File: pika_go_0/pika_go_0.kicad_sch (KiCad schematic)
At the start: 0 parts

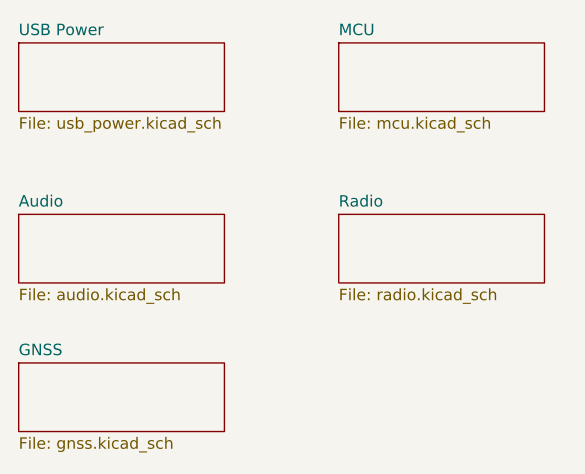
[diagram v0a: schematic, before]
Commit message: Libraries cleanup, schematics finished, copper tracing finished, still need some PCB cleanup
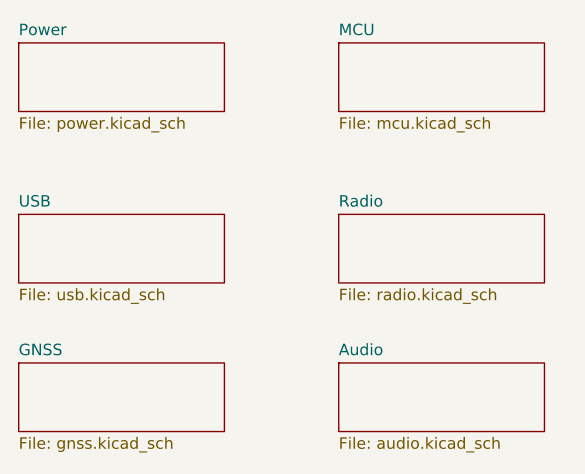
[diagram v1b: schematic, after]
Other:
- sheet USB Power renamed USB
- added sheet Power (power.kicad_sch)
- sheet USB: file usb_power.kicad_sch -> usb.kicad_sch
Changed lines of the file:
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@@
 	(paper "A4")
+	(sheet
+		(at 21.59 21.59)
+		(size 22.86 7.62)
+		(exclude_from_sim no)
+		(in_bom yes)
+		(on_board yes)
+		(dnp no)
+		(fields_autoplaced yes)
+		(stroke
+			(width 0.1524)
+			(type solid)
+		)
+		(fill
+			(color 0 0 0 0)
+		)
+		(property "Sheetname" "Power"
+			(at 21.59 20.8784 0)
+			(show_name no)
+			(do_not_autoplace no)
+			(effects
+				(font
+					(size 1.27 1.27)
+				)
+				(justify left bottom)
+			)
+		)
+		(property "Sheetfile" "power.kicad_sch"
+			(at 21.59 29.7946 0)
+			(show_name no)
+			(do_not_autoplace no)
+			(effects
+				(font
+					(size 1.27 1.27)
+				)
+				(justify left top)
+			)
+		)
+		(instances
+			(project "pika_go_0"
+				(path "/71487f0a-8ca7-4aa8-8af1-384680074486"
+					(page "2")
+				)
+			)
+		)
+	)
 	(sheet
 		(at 57.15 40.64)
@@
 	)
 	(sheet
+		(at 57.15 57.15)
+		(size 22.86 7.62)
+		(exclude_from_sim no)
+		(in_bom yes)
+		(on_board yes)
+		(dnp no)
+		(fields_autoplaced yes)
+		(stroke
+			(width 0.1524)
+			(type solid)
+		)
+		(fill
+			(color 0 0 0 0)
+		)
+		(property "Sheetname" "Audio"
+			(at 57.15 56.4384 0)
+			(show_name no)
+			(do_not_autoplace no)
+			(effects
+				(font
+					(size 1.27 1.27)
+				)
+				(justify left bottom)
+			)
+		)
+		(property "Sheetfile" "audio.kicad_sch"
+			(at 57.15 65.3546 0)
+			(show_name no)
+			(do_not_autoplace no)
+			(effects
+				(font
+					(size 1.27 1.27)
+				)
+				(justify left top)
+			)
+		)
+		(instances
+			(project "pika_go_0"
+				(path "/71487f0a-8ca7-4aa8-8af1-384680074486"
+					(page "7")
+				)
+			)
+		)
+	)
+	(sheet
 		(at 21.59 40.64)
 		(size 22.86 7.62)
@@
 			(color 0 0 0 0)
 		)
-		(property "Sheetname" "Audio"
+		(property "Sheetname" "USB"
 			(at 21.59 39.9284 0)
 			(show_name no)
@@
 			)
 		)
-		(property "Sheetfile" "audio.kicad_sch"
+		(property "Sheetfile" "usb.kicad_sch"
 			(at 21.59 48.8446 0)
 			(show_name no)
@@
 				)
 			)
-		)
-	)
-	(sheet
-		(at 21.59 21.59)
-		(size 22.86 7.62)
-		(exclude_from_sim no)
-		(in_bom yes)
-		(on_board yes)
-		(dnp no)
-		(fields_autoplaced yes)
-		(stroke
-			(width 0.1524)
-			(type solid)
-		)
-		(fill
-			(color 0 0 0 0)
-		)
-		(property "Sheetname" "USB Power"
-			(at 21.59 20.8784 0)
-			(show_name no)
-			(do_not_autoplace no)
-			(effects
-				(font
-					(size 1.27 1.27)
-				)
-				(justify left bottom)
-			)
-		)
-		(property "Sheetfile" "usb_power.kicad_sch"
-			(at 21.59 29.7946 0)
-			(show_name no)
-			(do_not_autoplace no)
-			(effects
-				(font
-					(size 1.27 1.27)
-				)
-				(justify left top)
-			)
-		)
-		(instances
-			(project "pika_go_0"
-				(path "/71487f0a-8ca7-4aa8-8af1-384680074486"
-					(page "2")
-				)
-			)
